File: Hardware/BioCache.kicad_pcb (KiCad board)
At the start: 2 copper layers, 58.8 x 80.6 mm, 44 parts, among them J1 Conn_01x16_Male, J10 Conn_01x04_Male, J11 Conn_01x05_Male, J12 Conn_01x04_Male, J13 Conn_01x01_Male, J14 Conn_01x02_Male, J15 Conn_01x01_Male, J16 Conn_01x01_Male, J17 Conn_01x01_Male, J18 Conn_01x01_Male, J19 Conn_01x02_Male, J2 Conn_01x16_Male, J20 Conn_01x02_Male, J21 Conn_01x02_Male, J22 Conn_01x01_Male, J23 Conn_01x01_Male, J24 Conn_01x01_Male, J25 Conn_01x01_Male, J3 Conn_01x14_Male, J4 Conn_01x14_Male, J5 Conn_01x04_Male, J6 Conn_01x05_Male, J7 Conn_01x05_Male, J8 Conn_01x04_Male, J9 Conn_01x05_Male, U1 61C1024, U2 61C1024, U3 61C1024, U4 61C1024, U5 61C1024, U6 61C1024, U7 61C1024, U8 61C1024, U9 61C1024

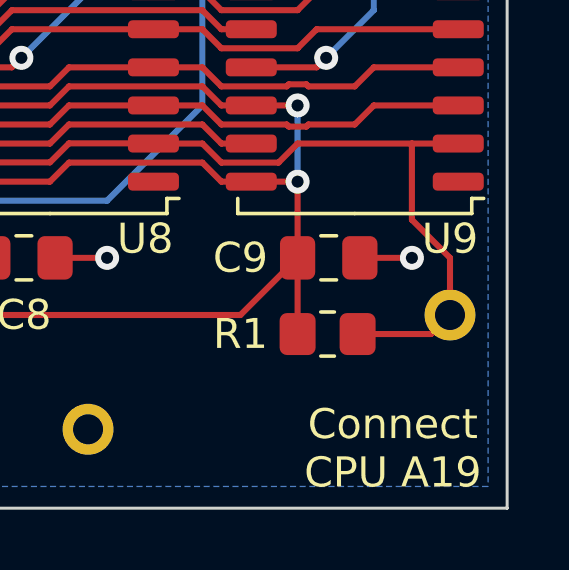
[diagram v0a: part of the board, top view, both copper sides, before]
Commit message: Upgrade to KiCad 9, clean-up schematics, set up KiBot
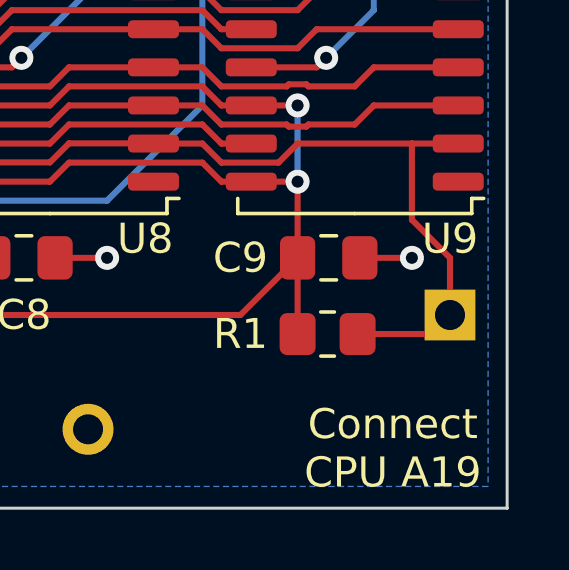
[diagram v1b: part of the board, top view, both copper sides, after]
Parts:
- J1.1: renamed from J8; footprint Connector_PinHeader_2.54mm:PinHeader_1x04_P2.54mm_Vertical -> ConnectorNoSquare1:PinHeader_1x04_P2.54mm_Vertical_NoSquare1
- J1.2: renamed from J9; footprint Connector_PinHeader_2.54mm:PinHeader_1x05_P2.54mm_Vertical -> ConnectorNoSquare1:PinHeader_1x05_P2.54mm_Vertical_NoSquare1
- J1.3: renamed from J18; footprint Connector_PinHeader_2.54mm:PinHeader_1x01_P2.54mm_Vertical -> ConnectorNoSquare1:PinHeader_1x01_P2.54mm_Vertical_NoSquare1
- J10.1: renamed from J24; footprint Connector_PinHeader_2.54mm:PinHeader_1x01_P2.54mm_Vertical -> ConnectorNoSquare1:PinHeader_1x01_P2.54mm_Vertical_NoSquare1
- J10.2: renamed from J25; footprint Connector_PinHeader_2.54mm:PinHeader_1x01_P2.54mm_Vertical -> ConnectorNoSquare1:PinHeader_1x01_P2.54mm_Vertical_NoSquare1
- J10.3: renamed from J20; footprint Connector_PinHeader_2.54mm:PinHeader_1x02_P2.54mm_Vertical -> ConnectorNoSquare1:PinHeader_1x02_P2.54mm_Vertical_NoSquare1
- J11.1: renamed from J23; footprint Connector_PinHeader_2.54mm:PinHeader_1x01_P2.54mm_Vertical -> ConnectorNoSquare1:PinHeader_1x01_P2.54mm_Vertical_NoSquare1
- J11.2: renamed from J19; footprint Connector_PinHeader_2.54mm:PinHeader_1x02_P2.54mm_Vertical -> ConnectorNoSquare1:PinHeader_1x02_P2.54mm_Vertical_NoSquare1
- J12.1: renamed from J3; footprint Connector_PinHeader_2.54mm:PinHeader_1x14_P2.54mm_Vertical -> ConnectorNoSquare1:PinHeader_1x14_P2.54mm_Vertical_NoSquare1
- J12.2: renamed from J14; footprint Connector_PinHeader_2.54mm:PinHeader_1x02_P2.54mm_Vertical -> ConnectorNoSquare1:PinHeader_1x02_P2.54mm_Vertical_NoSquare1
- J13.1: renamed from J22; footprint Connector_PinHeader_2.54mm:PinHeader_1x01_P2.54mm_Vertical -> ConnectorNoSquare1:PinHeader_1x01_P2.54mm_Vertical_NoSquare1
- J13.2: renamed from J4; footprint Connector_PinHeader_2.54mm:PinHeader_1x14_P2.54mm_Vertical -> ConnectorNoSquare1:PinHeader_1x14_P2.54mm_Vertical_NoSquare1
- J2.1: renamed from J12; footprint Connector_PinHeader_2.54mm:PinHeader_1x04_P2.54mm_Vertical -> ConnectorNoSquare1:PinHeader_1x04_P2.54mm_Vertical_NoSquare1
- J2.2: renamed from J7; footprint Connector_PinHeader_2.54mm:PinHeader_1x05_P2.54mm_Vertical -> ConnectorNoSquare1:PinHeader_1x05_P2.54mm_Vertical_NoSquare1
- J2.3: renamed from J17; footprint Connector_PinHeader_2.54mm:PinHeader_1x01_P2.54mm_Vertical -> ConnectorNoSquare1:PinHeader_1x01_P2.54mm_Vertical_NoSquare1
- J3.1: renamed from J2; footprint Connector_PinHeader_2.54mm:PinHeader_1x16_P2.54mm_Vertical -> ConnectorNoSquare1:PinHeader_1x16_P2.54mm_Vertical_NoSquare1
- J3.2: renamed from J6; footprint Connector_PinHeader_2.54mm:PinHeader_1x05_P2.54mm_Vertical -> ConnectorNoSquare1:PinHeader_1x05_P2.54mm_Vertical_NoSquare1
- J3.3: renamed from J13; footprint Connector_PinHeader_2.54mm:PinHeader_1x01_P2.54mm_Vertical -> ConnectorNoSquare1:PinHeader_1x01_P2.54mm_Vertical_NoSquare1
- J4.1: renamed from J16; footprint Connector_PinHeader_2.54mm:PinHeader_1x01_P2.54mm_Vertical -> ConnectorNoSquare1:PinHeader_1x01_P2.54mm_Vertical_NoSquare1
- J4.2: renamed from J5; footprint Connector_PinHeader_2.54mm:PinHeader_1x04_P2.54mm_Vertical -> ConnectorNoSquare1:PinHeader_1x04_P2.54mm_Vertical_NoSquare1
- J4.3: renamed from J1; footprint Connector_PinHeader_2.54mm:PinHeader_1x16_P2.54mm_Vertical -> ConnectorNoSquare1:PinHeader_1x16_P2.54mm_Vertical_NoSquare1
- J8.1: renamed from J10; footprint Connector_PinHeader_2.54mm:PinHeader_1x04_P2.54mm_Vertical -> ConnectorNoSquare1:PinHeader_1x04_P2.54mm_Vertical_NoSquare1
- J8.2: renamed from J11; footprint Connector_PinHeader_2.54mm:PinHeader_1x05_P2.54mm_Vertical -> ConnectorNoSquare1:PinHeader_1x05_P2.54mm_Vertical_NoSquare1
- J8.3: renamed from J21; footprint Connector_PinHeader_2.54mm:PinHeader_1x02_P2.54mm_Vertical -> ConnectorNoSquare1:PinHeader_1x02_P2.54mm_Vertical_NoSquare1
- renumbered J15 to JA19
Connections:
- net A18 renamed /Data RAM/A18
- net A19 renamed /Data RAM/A19
- net AA10 renamed /Data RAM/AA10
- net AA11 renamed /Data RAM/AA11
- net AA12 renamed /Data RAM/AA12
- net AA13 renamed /Data RAM/AA13
- net AA14 renamed /Data RAM/AA14
- net AA15 renamed /Data RAM/AA15
- net AA16 renamed /Data RAM/AA16
- net AA17 renamed /Data RAM/AA17
- net AA4 renamed /Data RAM/AA4
- net AA5 renamed /Data RAM/AA5
- net AA6 renamed /Data RAM/AA6
- net AA7 renamed /Data RAM/AA7
- net AA8 renamed /Data RAM/AA8
- net AA9 renamed /Data RAM/AA9
- net AB10 renamed /Data RAM/AB10
- net AB11 renamed /Data RAM/AB11
- net AB12 renamed /Data RAM/AB12
- net AB13 renamed /Data RAM/AB13
- net AB14 renamed /Data RAM/AB14
- net AB15 renamed /Data RAM/AB15
- net AB16 renamed /Data RAM/AB16
- net AB17 renamed /Data RAM/AB17
- net AB4 renamed /Data RAM/AB4
- net AB5 renamed /Data RAM/AB5
- net AB6 renamed /Data RAM/AB6
- net AB7 renamed /Data RAM/AB7
- net AB8 renamed /Data RAM/AB8
- net AB9 renamed /Data RAM/AB9
- net D0 renamed /Data RAM/D0
- net D1 renamed /Data RAM/D1
- net D10 renamed /Data RAM/D10
- net D11 renamed /Data RAM/D11
- net D12 renamed /Data RAM/D12
- net D13 renamed /Data RAM/D13
- net D14 renamed /Data RAM/D14
- net D15 renamed /Data RAM/D15
- net D16 renamed /Data RAM/D16
- net D17 renamed /Data RAM/D17
- net D18 renamed /Data RAM/D18
- net D19 renamed /Data RAM/D19
- net D2 renamed /Data RAM/D2
- net D20 renamed /Data RAM/D20
- net D21 renamed /Data RAM/D21
- net D22 renamed /Data RAM/D22
- net D23 renamed /Data RAM/D23
- net D24 renamed /Data RAM/D24
- net D25 renamed /Data RAM/D25
- net D26 renamed /Data RAM/D26
- net D27 renamed /Data RAM/D27
- net D28 renamed /Data RAM/D28
- net D29 renamed /Data RAM/D29
- net D3 renamed /Data RAM/D3
- net D30 renamed /Data RAM/D30
- net D31 renamed /Data RAM/D31
- net D4 renamed /Data RAM/D4
- net D5 renamed /Data RAM/D5
- net D6 renamed /Data RAM/D6
- net D7 renamed /Data RAM/D7
- net D8 renamed /Data RAM/D8
- net D9 renamed /Data RAM/D9
- net KAA0 renamed /Data RAM/KAA0
- net KAB0 renamed /Data RAM/KAB0
- net TD0 renamed /Tag RAM and Connectors/TD0
- net TD1 renamed /Tag RAM and Connectors/TD1
- net TD2 renamed /Tag RAM and Connectors/TD2
- net TD3 renamed /Tag RAM and Connectors/TD3
- net TD4 renamed /Tag RAM and Connectors/TD4
- net TD5 renamed /Tag RAM and Connectors/TD5
- net TD6 renamed /Tag RAM and Connectors/TD6
- net TD7 renamed /Tag RAM and Connectors/TD7
- net VCCA renamed /Tag RAM and Connectors/VCCA
- net VCCB renamed /Tag RAM and Connectors/VCCB
- net ~{KCEA} renamed /Data RAM/~{KCEA}
- net ~{KCEB} renamed /Data RAM/~{KCEB}
- net ~{KOEA} renamed /Data RAM/~{KOEA}
- net ~{KOEB} renamed /Data RAM/~{KOEB}
- net ~{KWE1} renamed /Data RAM/~{KWE1}
- net ~{KWE2} renamed /Data RAM/~{KWE2}
- net ~{KWE3} renamed /Data RAM/~{KWE3}
- net ~{KWEA0} renamed /Data RAM/~{KWEA0}
- net ~{KWEB0} renamed /Data RAM/~{KWEB0}
- net ~{TWE} renamed /Tag RAM and Connectors/TWE

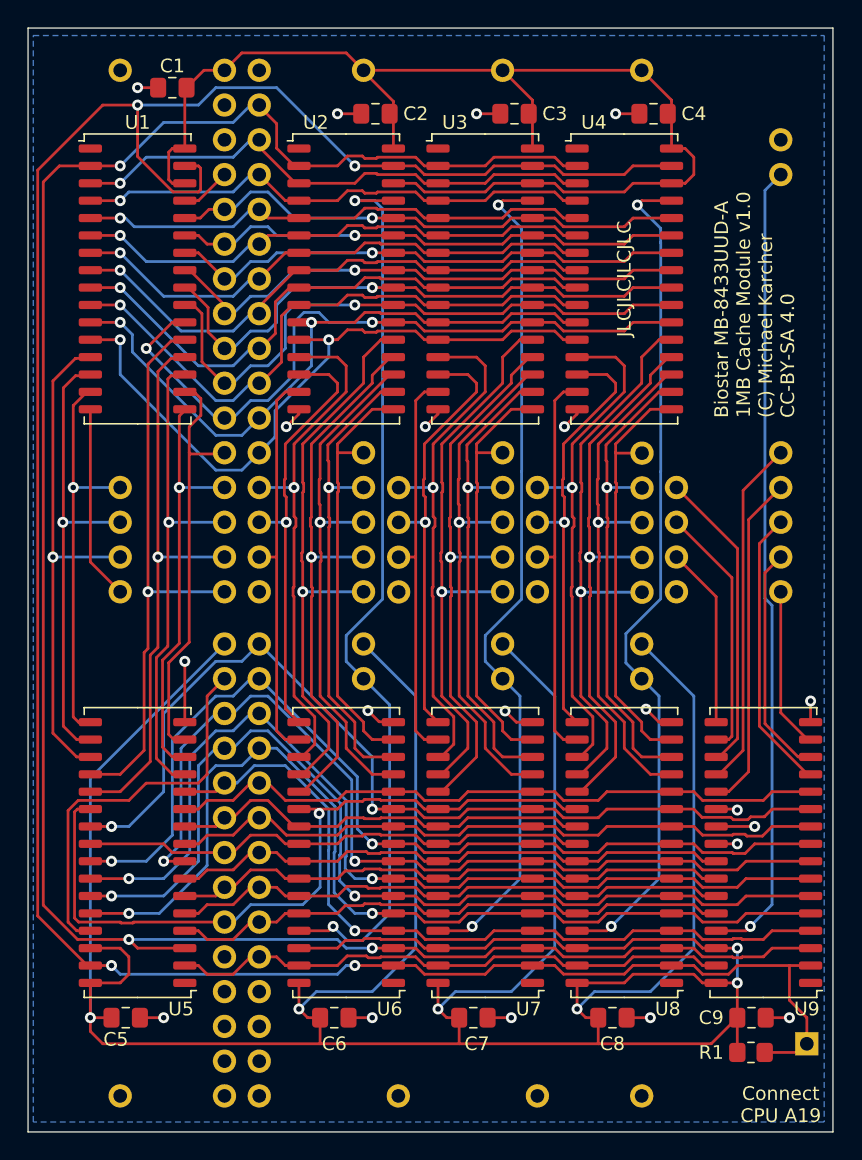
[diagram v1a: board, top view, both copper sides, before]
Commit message: Ûpdate SOJ32 footprints to wider layout
Reroute traces as required.
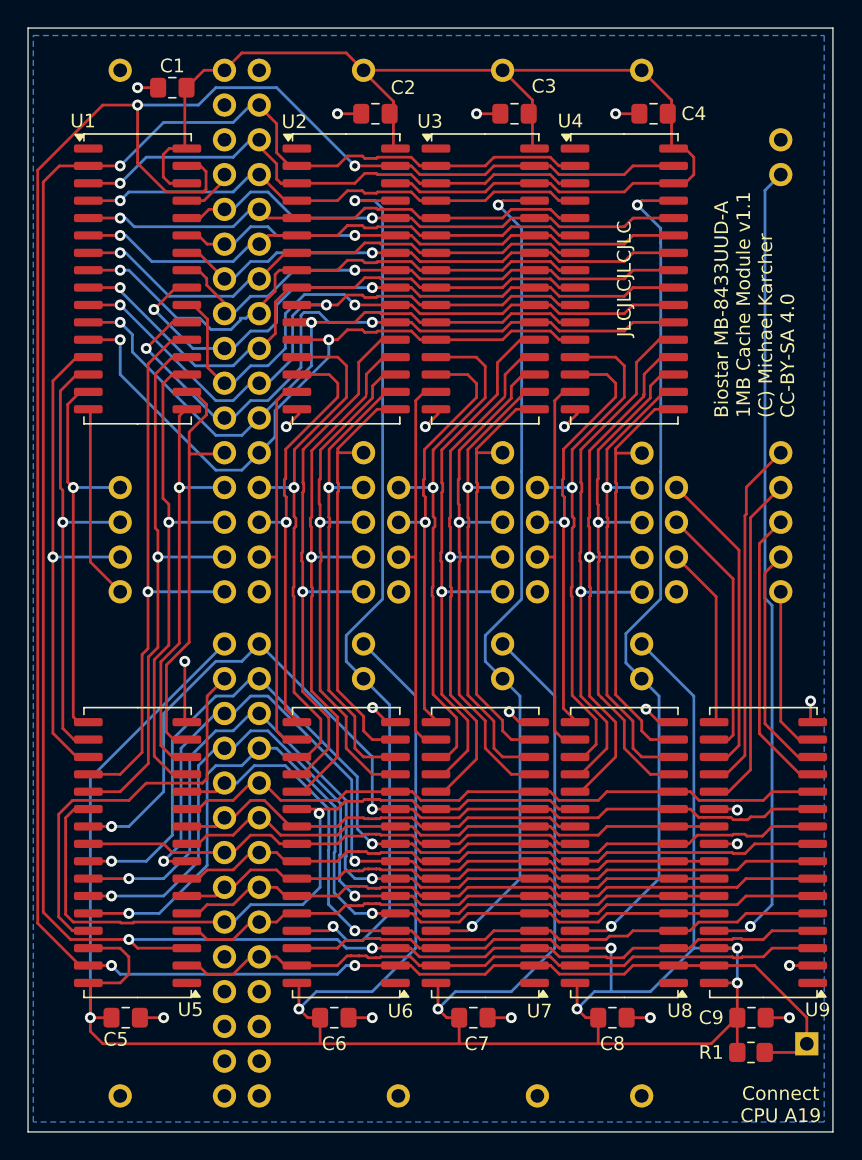
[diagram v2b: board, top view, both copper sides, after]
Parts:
- U1, U2, U3, U4, U5, U6, U7, U8, U9: footprint Package_SOJ:SOJ-32_7.58x20.955mm_P1.27mm -> Package_SO:SOJ-32_7.62x20.955mm_P1.27mm
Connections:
- U9 pad 10: /Data RAM/AB12 -> /Data RAM/AB8
- U9 pad 2: /Data RAM/A19 -> GND
- U9 pad 23: GND -> /Data RAM/AB12
- U9 pad 25: /Data RAM/AB16 -> /Data RAM/AB15
- U9 pad 26: /Data RAM/AB17 -> /Data RAM/AB9
- U9 pad 27: /Data RAM/AB14 -> /Data RAM/AB5
- U9 pad 28: /Data RAM/AB6 -> /Data RAM/AB10
- U9 pad 3: /Data RAM/A18 -> /Data RAM/AB7
- U9 pad 31: /Data RAM/AB7 -> /Data RAM/A19
- U9 pad 4: /Data RAM/AB4 -> /Data RAM/A18
- U9 pad 5: /Data RAM/AB10 -> /Data RAM/AB4
- U9 pad 6: /Data RAM/AB5 -> /Data RAM/AB6
- U9 pad 7: /Data RAM/AB9 -> /Data RAM/AB14
- U9 pad 8: /Data RAM/AB15 -> /Data RAM/AB17
- U9 pad 9: /Data RAM/AB8 -> /Data RAM/AB16
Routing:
- net /Tag RAM and Connectors/VCCB: track 265.2 -> 252.7 mm, vias 6 -> 7
- net /Data RAM/AB12: track 49.0 -> 41.5 mm
- net /Data RAM/AB5: track 71.7 -> 64.3 mm
- net /Data RAM/AB9: track 71.3 -> 63.9 mm
- net /Data RAM/AB15: track 67.8 -> 60.4 mm
- net /Data RAM/AB10: track 71.9 -> 64.4 mm
- net /Data RAM/AB16: track 41.6 -> 48.5 mm
- net /Data RAM/AB7: track 41.6 -> 48.5 mm
- net /Data RAM/AB6: track 41.5 -> 48.4 mm
- net /Data RAM/AB14: track 41.6 -> 48.5 mm
- net /Data RAM/AB17: track 41.5 -> 48.4 mm
- net /Data RAM/~{KOEA}: track 42.1 -> 45.6 mm, vias 1 -> 2
- net /Data RAM/AA14: track 44.5 -> 46.9 mm, vias 1 -> 2
- net /Data RAM/A19: track 188.7 -> 186.3 mm
- net GND: track 52.7 -> 51.2 mm
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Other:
- board text added: "Biostar MB-8433UUD-A 1MB Cache Module v1.1 (C) Michael Karcher CC-BY-SA 4.0"
- board text removed: "Biostar MB-8433UUD-A 1MB Cache Module v1.0 (C) Michael Karcher CC-BY-SA 4.0"
